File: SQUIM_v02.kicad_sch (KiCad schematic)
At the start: 29 parts, among them J1 Conn_01x03, J2 Conn_Coaxial, J3 Conn_01x02_Socket, J4 Conn_01x04_Socket, J5 Conn_01x02_Socket, J6 Conn_01x04_Socket, SW1 reset, U1 RaspberryPi_Pico_W, U2 MAX98357A

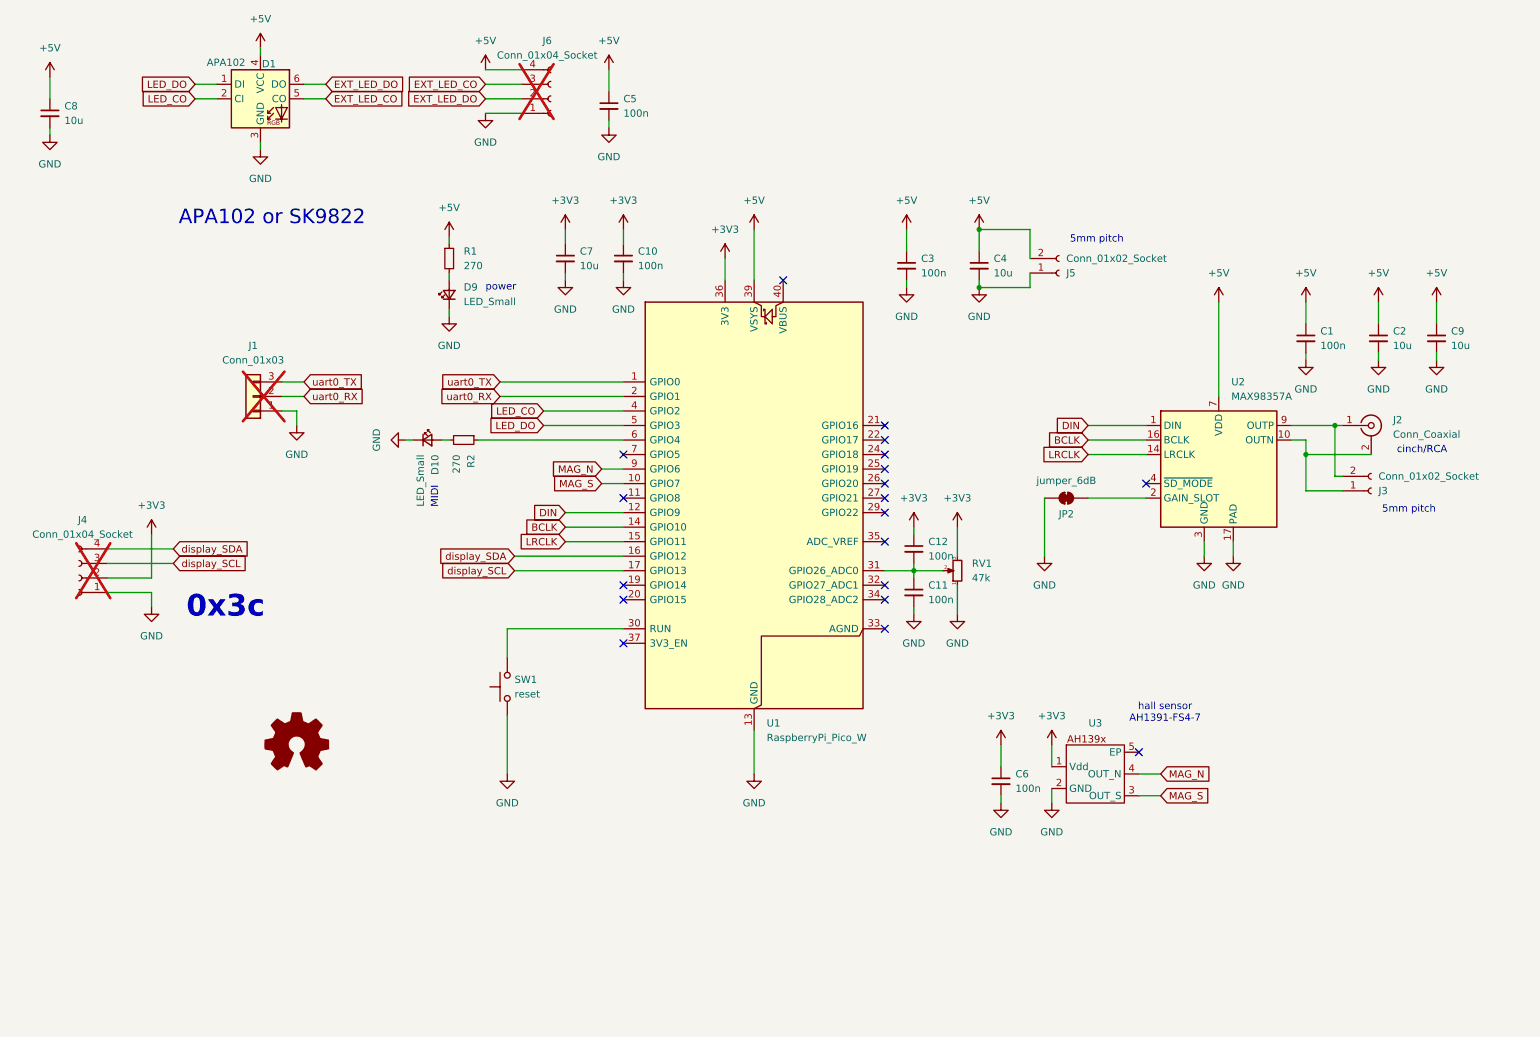
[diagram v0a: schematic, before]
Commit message: all the v1->v2 changes as documented in the schematic
Signed-off-by: matthias wenzel <wenzel@wenzellabs.de>
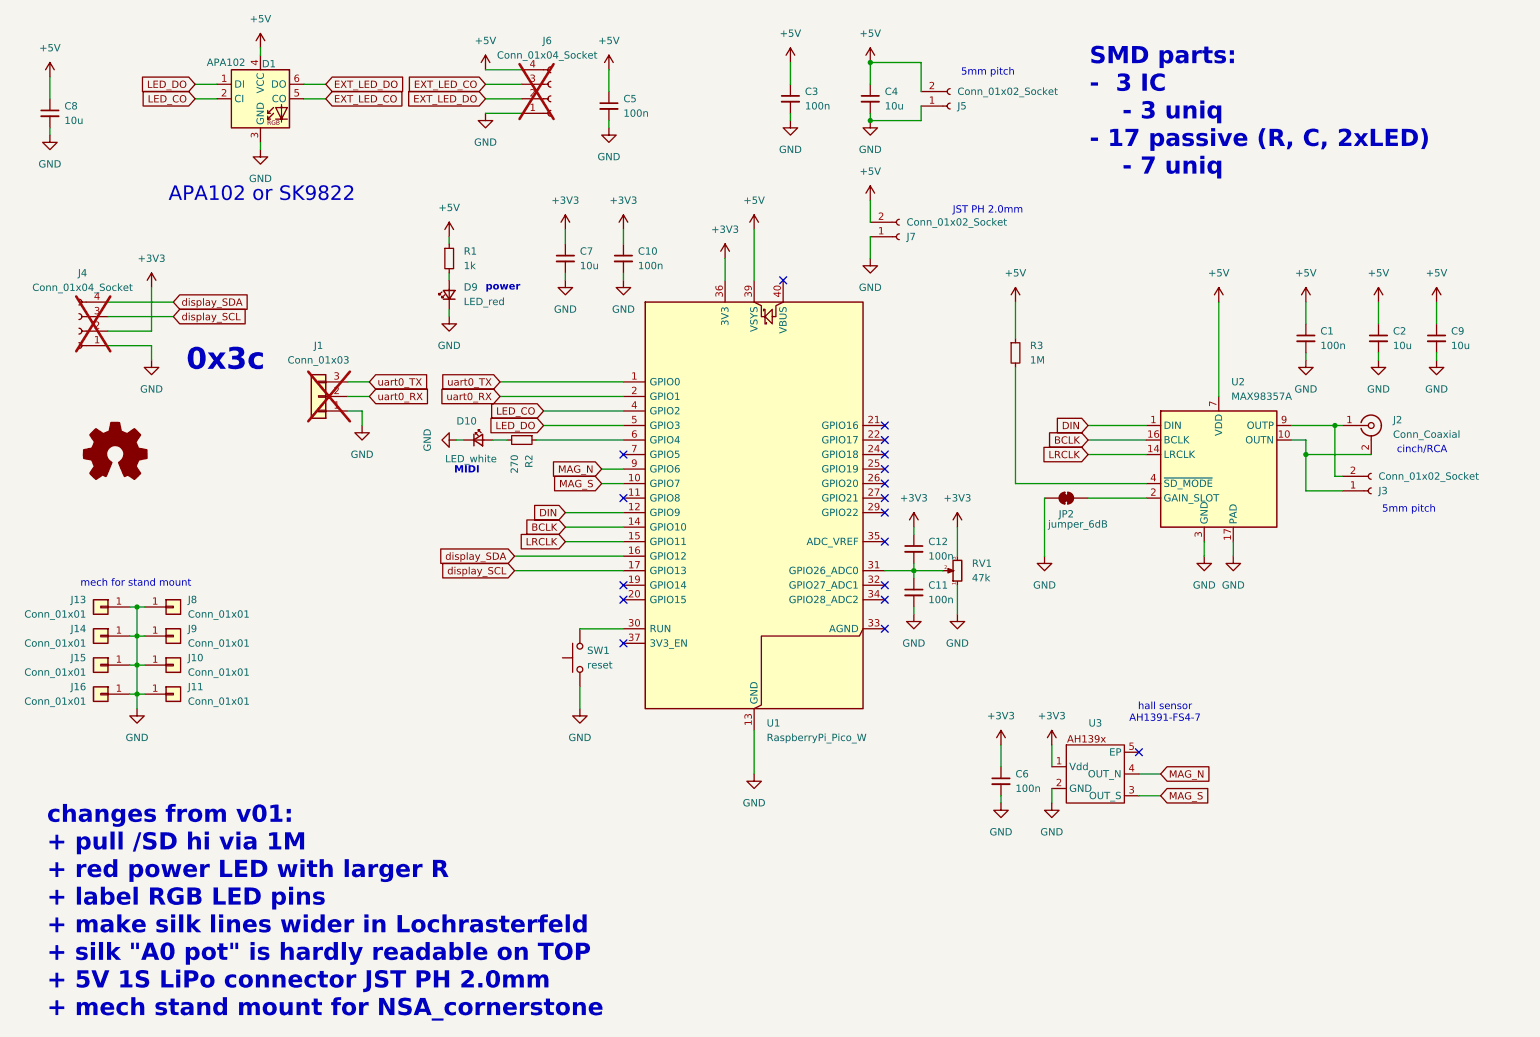
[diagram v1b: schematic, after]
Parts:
- added J10, J11, J13, J14, J15, J16, J8, J9: Conn_01x01, mazzoo:PCB_edge_pad_nopaste, symbol Connector_Generic:Conn_01x01
- added J7: Conn_01x02_Socket, Connector_JST:JST_PH_B2B-PH-K_1x02_P2.00mm_Vertical, symbol Connector:Conn_01x02_Socket
- added R3: 1M, Resistor_SMD:R_0603_1608Metric, symbol Device:R_Small
- D10: value LED_Small -> LED_white
- D9: value LED_Small -> LED_red
- R1: value 270 -> 1k
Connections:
- net +5V: now also J7.2 (Pin_2), R3.1
- net GND: now also J10.1 (Pin_1), J11.1 (Pin_1), J13.1 (Pin_1), J14.1 (Pin_1), J15.1 (Pin_1), J16.1 (Pin_1), J7.1 (Pin_1), J8.1 (Pin_1), J9.1 (Pin_1)
- net at U2.4 (~{SD_MODE}): now also R3.2
- no-connect marks 19 -> 18
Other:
- note added: "JST PH 2.0mm"
- note added: "SMD parts: - 3 IC - 3 uniq - 17 passive (R, C, 2xLED) - 7 uniq"
- note added: "changes from v01: + pull /SD hi via 1M + red power LED with larger R + label RGB LED pins + make silk lines wider in Lochrasterfeld + silk "A0 pot" is hardly readable on TOP + 5V 1S LiPo connector JST PH 2.0mm + mech stand mount for NSA_cornerstone"
- note added: "mech for stand mount"
- moved on the sheet: C3, C4, D10, J1, J4, J5, R2, SW1

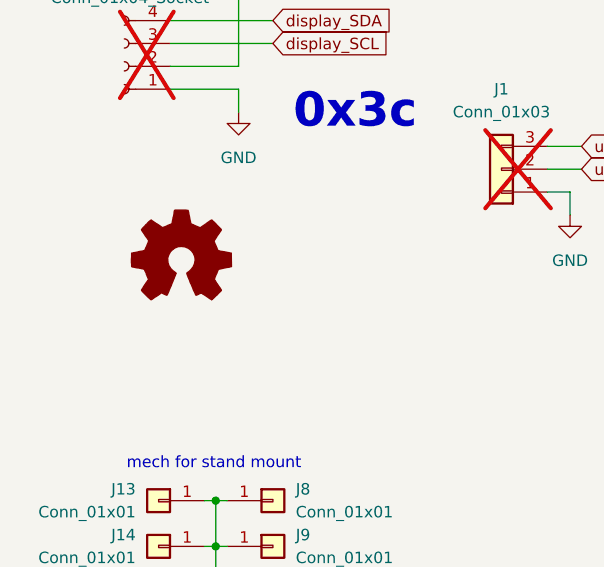
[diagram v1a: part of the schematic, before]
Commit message: add features description, pdf schematic
Signed-off-by: matthias wenzel <wenzel@wenzellabs.de>
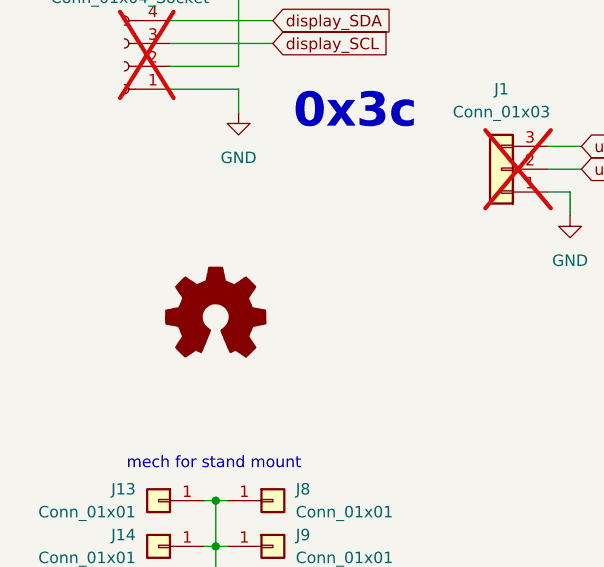
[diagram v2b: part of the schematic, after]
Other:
- company: (none) -> wenzellabs
- title: (none) -> SQUIM_v02
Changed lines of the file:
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@@
 	(generator_version "8.0")
 	(paper "A4")
+	(title_block
+		(title "SQUIM_v02")
+		(company "wenzellabs")
+	)
 	(junction
 		(at 165.1 31.75)
@@
 	(symbol
 		(lib_id "Graphic:Logo_Open_Hardware_Small")
-		(at 33.02 90.17 0)
+		(at 36.83 96.52 0)
 		(unit 1)
 		(exclude_from_sim yes)
@@
 		(fields_autoplaced yes)
 		(property "Reference" "#SYM1"
-			(at 33.02 83.185 0)
+			(at 36.83 89.535 0)
 			(effects
 				(font
@@
 		)
 		(property "Value" "Logo_Open_Hardware_Small"
-			(at 33.02 95.885 0)
+			(at 36.83 102.235 0)
 			(effects
 				(font
@@
 		)
 		(property "Footprint" ""
-			(at 33.02 90.17 0)
+			(at 36.83 96.52 0)
 			(effects
 				(font
@@
 		)
 		(property "Datasheet" "~"
-			(at 33.02 90.17 0)
+			(at 36.83 96.52 0)
 			(effects
 				(font
@@
 		)
 		(property "Description" "Open Hardware logo, small"
-			(at 33.02 90.17 0)
+			(at 36.83 96.52 0)
 			(effects
 				(font
